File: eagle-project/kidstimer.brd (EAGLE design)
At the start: 100 x 80 mm, 7 parts

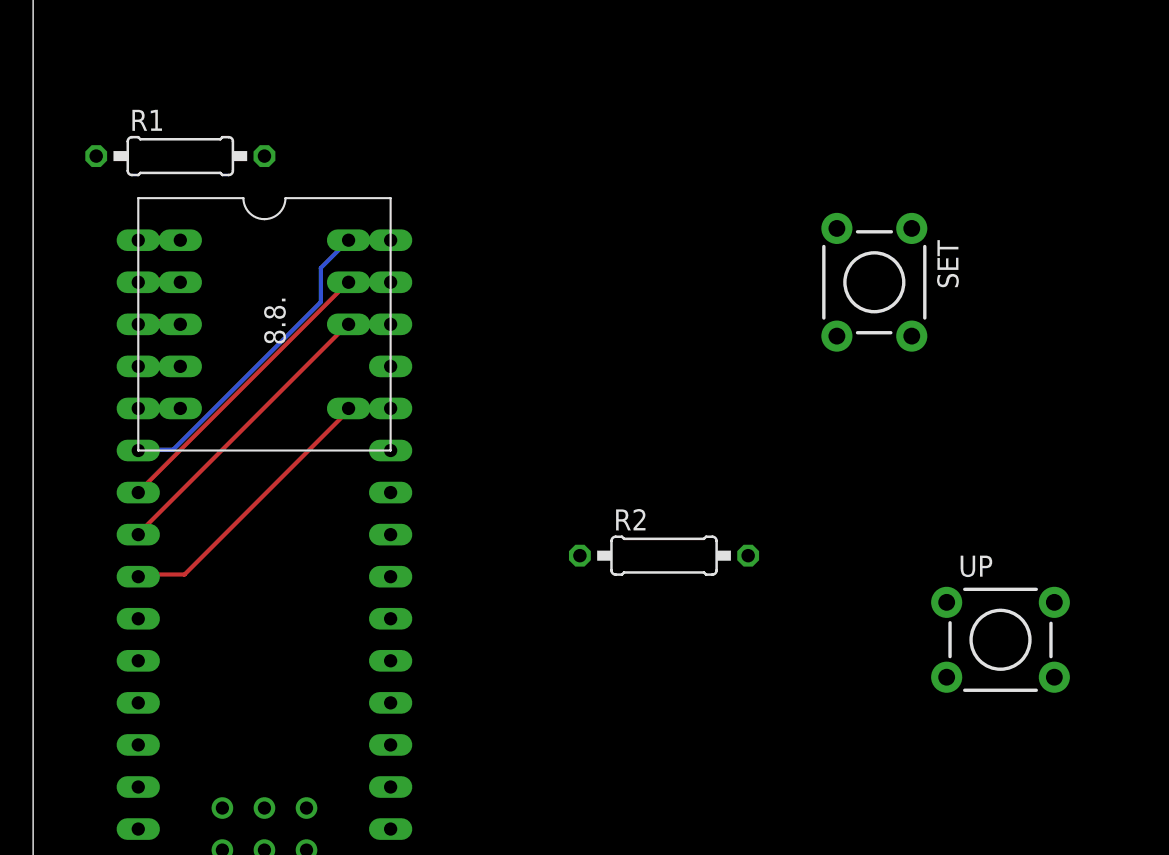
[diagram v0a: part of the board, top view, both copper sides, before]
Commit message: Changed pins after soldering
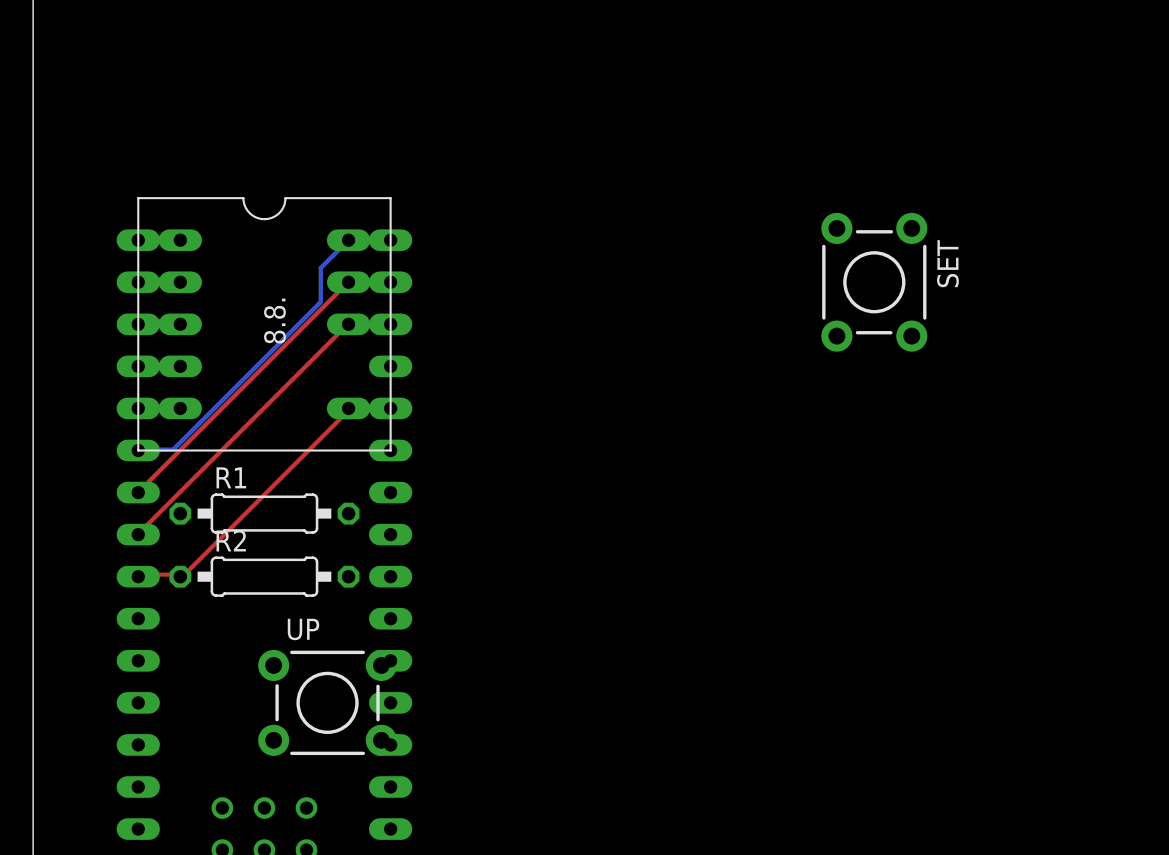
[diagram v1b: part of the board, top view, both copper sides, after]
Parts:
- moved UP 40.8 mm to (17.8, 25.4)
- moved R2 24.2 mm to (14.0, 33.0)
- moved R1 22.2 mm to (14.0, 36.8)
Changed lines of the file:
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@@
 <element name="U$2" library="Arduino-clone" package="NANO" value="NANO" x="11.43" y="26.67" rot="MR0"/>
 <element name="U$1" library="yair" package="DIP9" value="DDA302WL1DIP9" x="8.89" y="53.34"/>
-<element name="R1" library="rcl" package="0207/10" value="220" x="8.89" y="58.42"/>
-<element name="R2" library="rcl" package="0207/10" value="220" x="38.1" y="34.29"/>
-<element name="UP" library="SparkFun-Retired" package="TACTILE-PTH" value="" x="58.42" y="29.21"/>
+<element name="R1" library="rcl" package="0207/10" value="220" x="13.97" y="36.83"/>
+<element name="R2" library="rcl" package="0207/10" value="220" x="13.97" y="33.02"/>
+<element name="UP" library="SparkFun-Retired" package="TACTILE-PTH" value="" x="17.78" y="25.4"/>
 <element name="SET" library="SparkFun-Retired" package="TACTILE-PTH" value="" x="50.8" y="50.8" rot="R270"/>
 <element name="DOWN" library="SparkFun-Retired" package="TACTILE-PTH" value="" x="40.64" y="8.89"/>
@@
 <wire x1="19.05" y1="53.34" x2="17.3736" y2="51.6636" width="0.254" layer="16"/>
 <contactref element="R2" pad="2"/>
-<wire x1="17.3736" y1="49.6062" x2="43.18" y2="34.29" width="0" layer="19" extent="16-16"/>
+<wire x1="17.3736" y1="49.6062" x2="19.05" y2="33.02" width="0" layer="19" extent="16-16"/>
 </signal>
 <signal name="N$5">
 <contactref element="U$1" pad="P$5"/>
 <contactref element="R1" pad="2"/>
-<wire x1="8.89" y1="43.18" x2="13.97" y2="58.42" width="0" layer="19" extent="1-1"/>
+<wire x1="8.89" y1="43.18" x2="19.05" y2="36.83" width="0" layer="19" extent="1-1"/>
 </signal>
 <signal name="N$10">
 <contactref element="U$2" pad="D7"/>
 <contactref element="R2" pad="1"/>
-<wire x1="6.35" y1="40.64" x2="33.02" y2="34.29" width="0" layer="19" extent="1-1"/>
+<wire x1="6.35" y1="40.64" x2="8.89" y2="33.02" width="0" layer="19" extent="1-1"/>
 </signal>
 <signal name="N$11">
 <contactref element="R1" pad="1"/>
 <contactref element="U$2" pad="D8"/>
-<wire x1="6.35" y1="43.18" x2="3.81" y2="58.42" width="0" layer="19" extent="1-1"/>
+<wire x1="6.35" y1="43.18" x2="8.89" y2="36.83" width="0" layer="19" extent="1-1"/>
 </signal>
 <signal name="N$12">
 <contactref element="U$2" pad="D3"/>
 <contactref element="UP" pad="1"/>
-<wire x1="6.35" y1="30.48" x2="55.1688" y2="31.4706" width="0" layer="19" extent="1-1"/>
+<wire x1="6.35" y1="30.48" x2="14.5288" y2="27.6606" width="0" layer="19" extent="1-1"/>
 </signal>
 <signal name="N$13">
@@
 <contactref element="DOWN" pad="3"/>
 <contactref element="U$2" pad="GND1"/>
-<wire x1="37.3888" y1="6.6294" x2="55.1688" y2="26.9494" width="0" layer="19" extent="1-1"/>
+<wire x1="37.3888" y1="6.6294" x2="14.5288" y2="23.1394" width="0" layer="19" extent="1-1"/>
 <wire x1="6.35" y1="25.4" x2="37.3888" y2="6.6294" width="0" layer="19" extent="1-1"/>
 </signal>
